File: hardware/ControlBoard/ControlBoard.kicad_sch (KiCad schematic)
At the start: 122 parts, among them J1 Lamp 1 Out, J10 CAN, J11 USB_B_Micro, J12 Conn_01x02, J13 AVAILABLE GPIO, J14 MOTOR_CTRL1, J15 MOTOR_CTRL2, J2 ESTOP1, J3 ESTOP2, J4 Lamp 3 Out, J5 Lamp 2 Out, J6 Lamp 4 Out, J7 PWR_IN, J8 USB_B_Micro, J9 UART BACKUP, Q1 2N7002, Q2 2N7002, Q3 2N7002, Q4 2N7002, Q5 SS8050-G, Q6 SS8050-G, SW1 SW_Push, SW2 SW_Push, U1 CP2102N-A02-GQFN28, U2 Lora_Module, U5 ESP32-S3-WROOM-1U, U6 74LVC1G97W6-7, U7 SN65HVD232, U8 SN74LVC1GU04DBVR

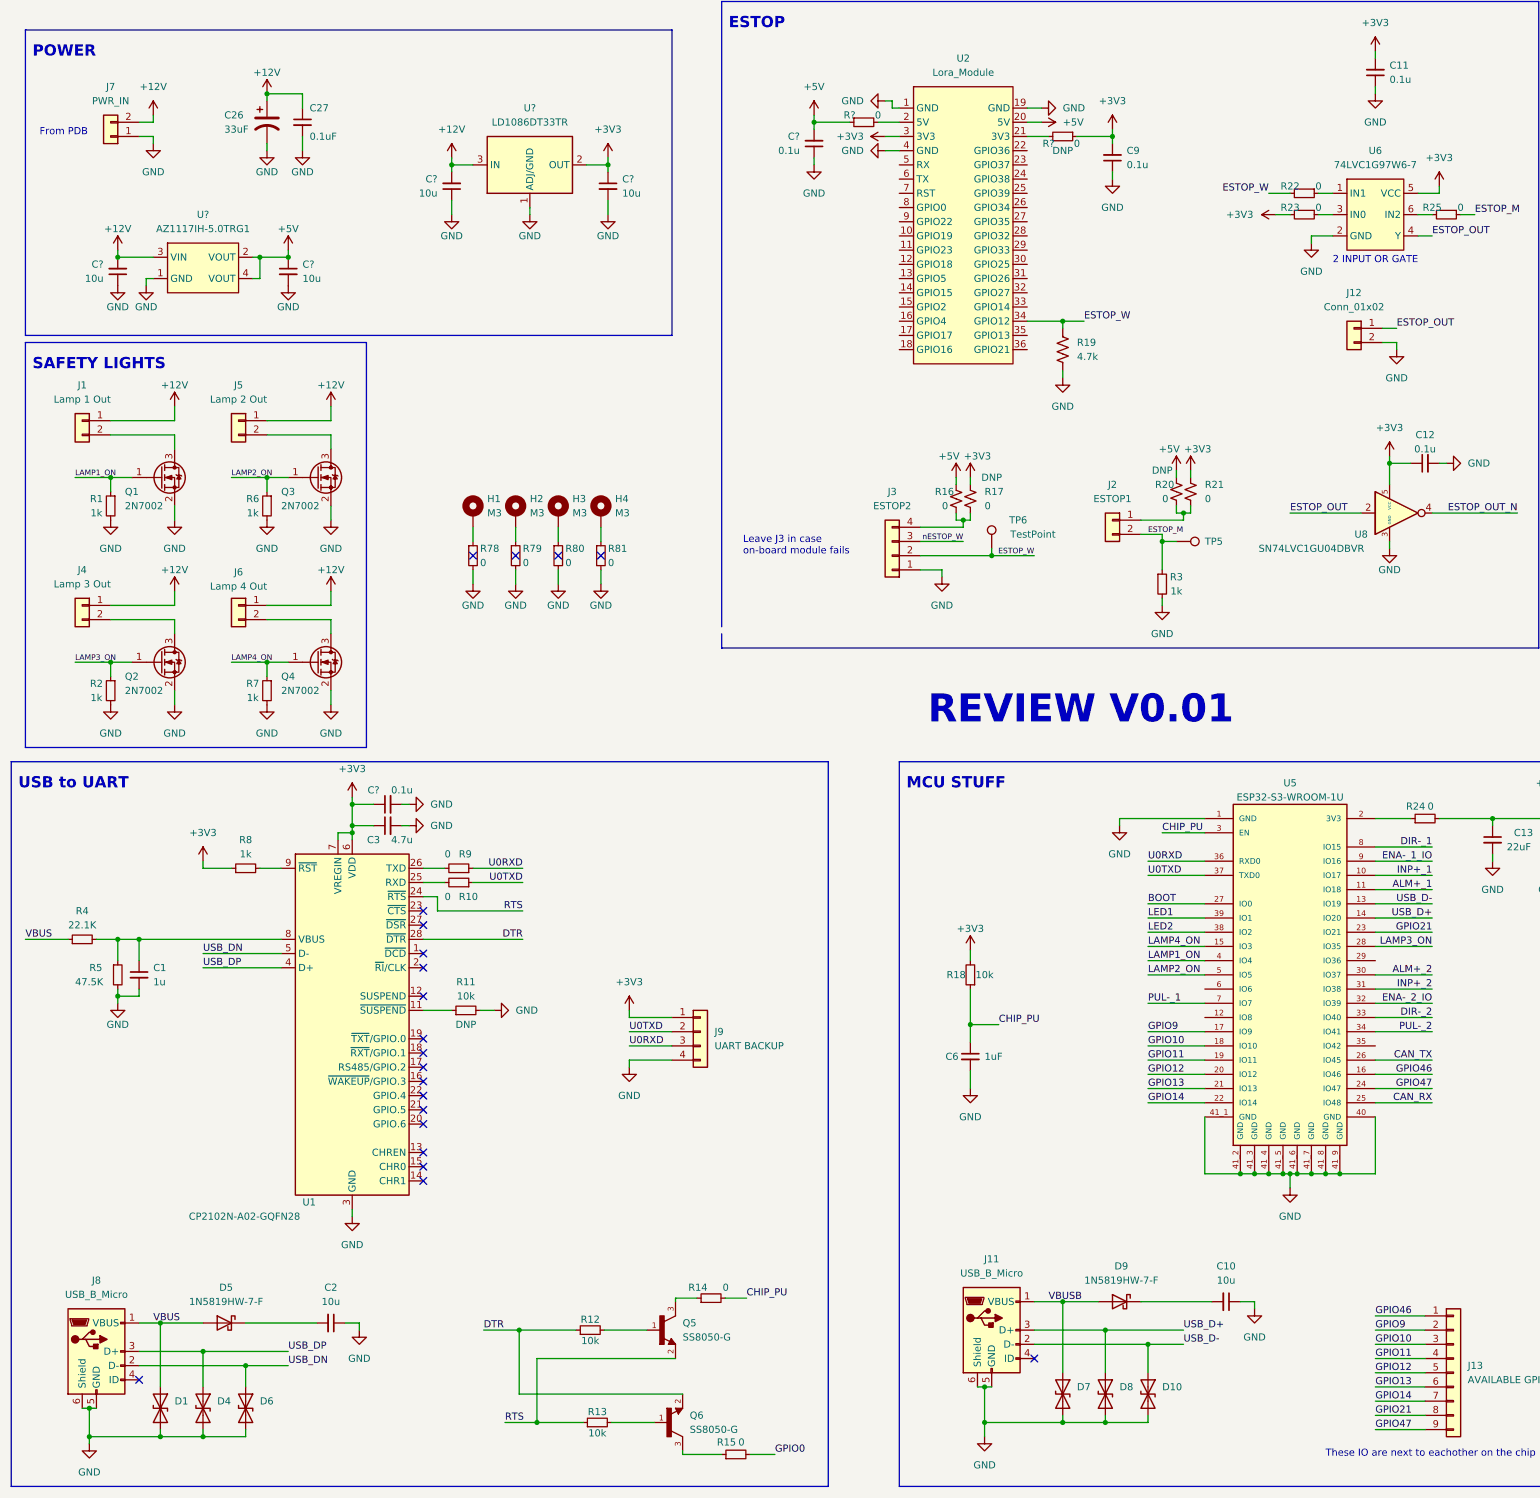
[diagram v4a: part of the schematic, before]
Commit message: Starting Control Board Layout
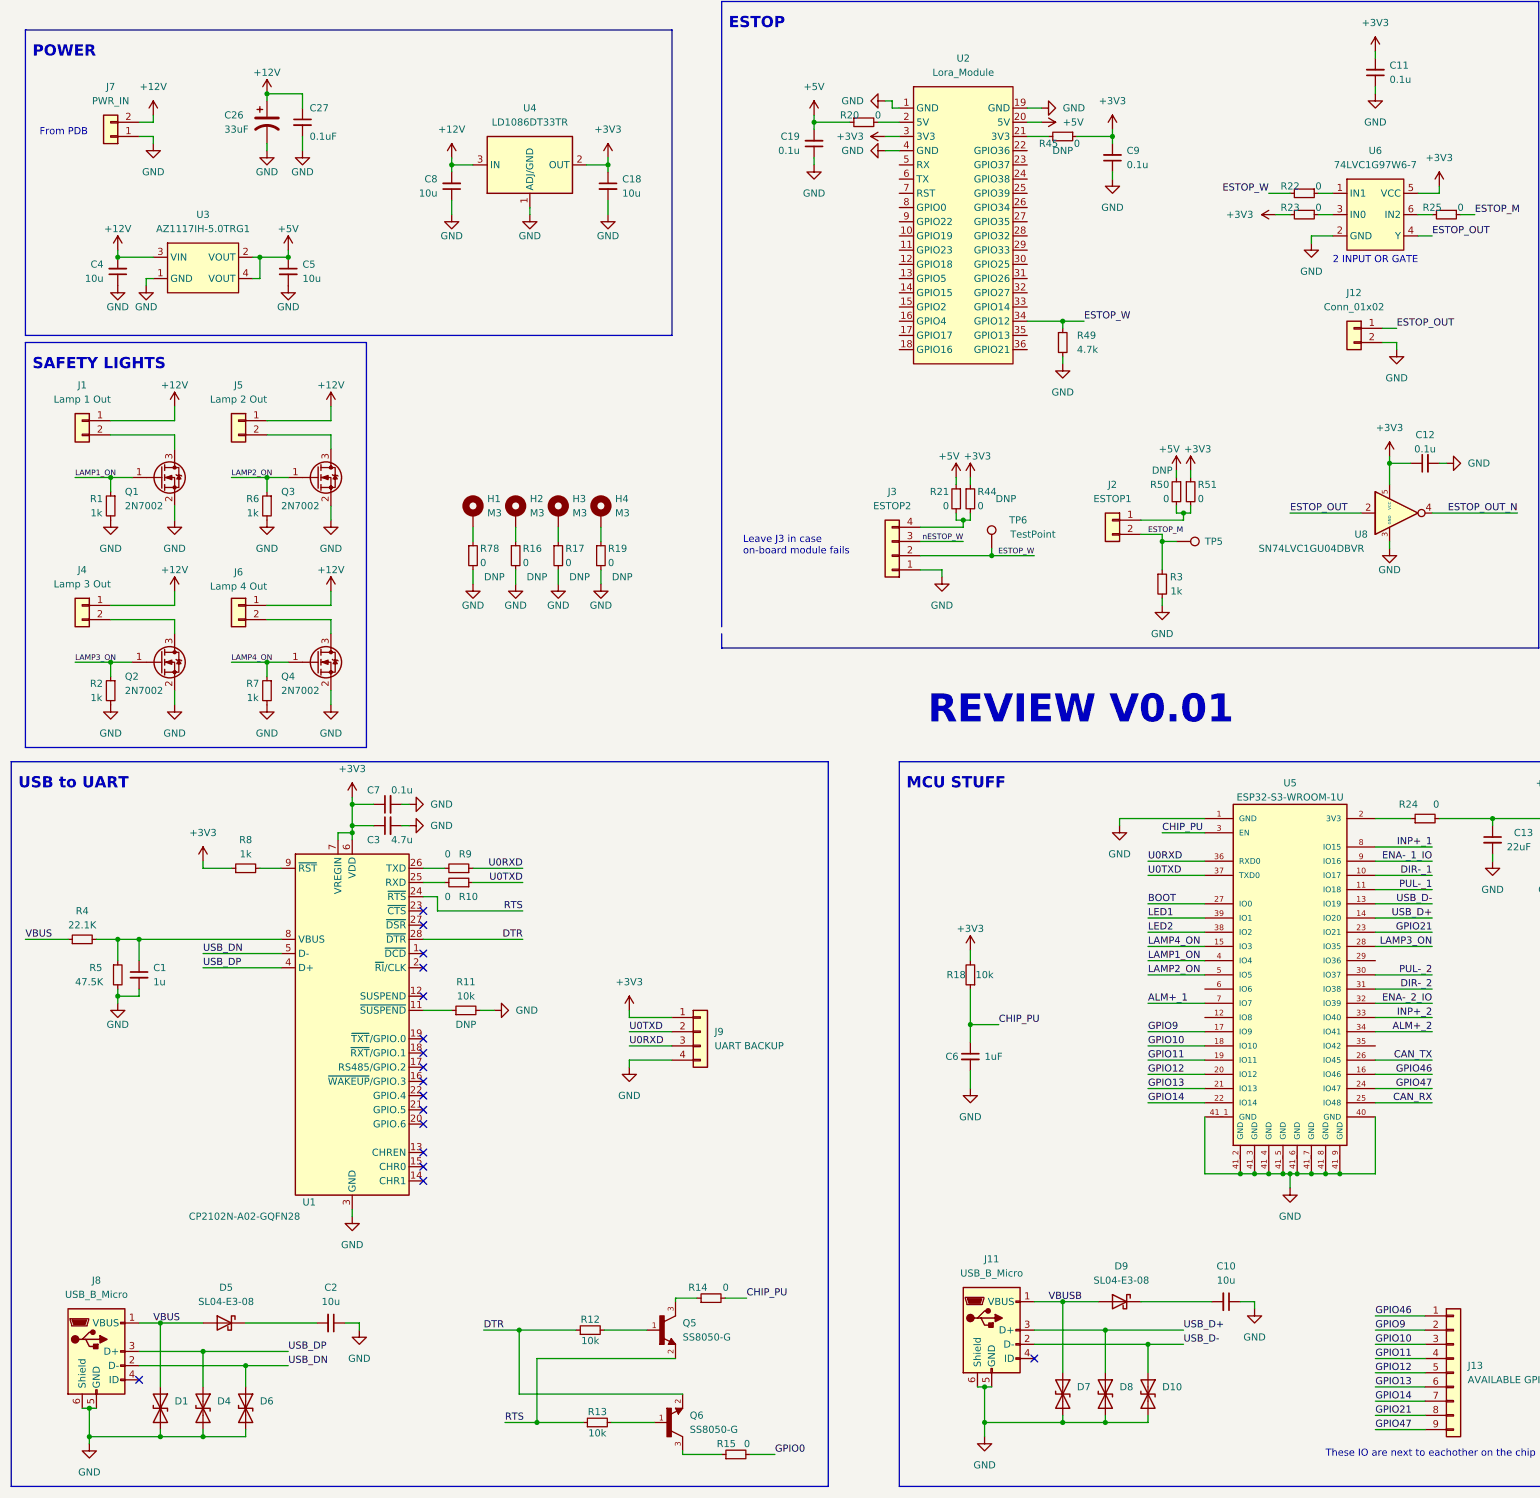
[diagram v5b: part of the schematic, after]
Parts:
- removed R16, R17, R20, R21: 0, symbol Device:R_Small_US
- removed R19: 4.7k, symbol Device:R_US
- removed R79, R80, R81: 0, Resistor_SMD:R_0603_1608Metric, symbol Device:R_Small
- added R16, R17, R19, R21, R44, R50, R51: 0, Resistor_SMD:R_0805_2012Metric, symbol Device:R_Small
- added R49: 4.7k, Resistor_SMD:R_0805_2012Metric, symbol Device:R_Small
- C1, C10, C11, C12, C2, C3, C9: footprint (none) -> Capacitor_SMD:C_0805_2012Metric
- C17: footprint Capacitor_SMD:C_0603_1608Metric -> Capacitor_SMD:C_0805_2012Metric
- C18, C19, C4, C5, C7, C8: renamed from C?; footprint (none) -> Capacitor_SMD:C_0805_2012Metric
- D5, D9: value 1N5819HW-7-F -> SL04-E3-08; footprint (none) -> Diode_SMD:D_SMF; Digikey 1N5819HW-FDICT-ND -> SL04-E3-08GICT-ND
- J11, J8: footprint (none) -> Connector_USB:USB_Micro-B_Molex-105017-0001; Digikey (none) -> WM1399CT-ND
- J7: footprint Connector_Molex:Molex_Mini-Fit_Sr_42820-22XX_1x02_P10.00mm_Horizontal -> Connector_Molex:Molex_Micro-Fit_3.0_43650-0200_1x02_P3.00mm_Horizontal; Digikey 0428202224-ND -> WM1860-ND
- R1, R10, R14, R15, R2, R24, R3, R6, R7, R75, R76, R9: footprint Resistor_SMD:R_0603_1608Metric -> Resistor_SMD:R_0805_2012Metric
- R11, R22, R23, R25, R26, R27, R28, R29, R30, R31, R32, R33, R34, R35, R36, R37, R38, R39, R4, R40, R41, R42, R43, R5, R8: footprint (none) -> Resistor_SMD:R_0805_2012Metric
- R20, R45: renamed from R?; footprint (none) -> Resistor_SMD:R_0805_2012Metric
- R46, R47: Digikey CR0603-JW-331ELFCT-ND -> (none)
- R48: footprint Resistor_SMD:R_0603_1608Metric -> Resistor_SMD:R_0805_2012Metric; Digikey A129677CT-ND -> (none)
- R78: footprint Resistor_SMD:R_0603_1608Metric -> Resistor_SMD:R_0805_2012Metric; DNP (none) -> DNP
- SW1, SW2: footprint (none) -> Button_Switch_SMD:SW_SPST_B3U-1100P-B; Digikey (none) -> SW1104CT-ND
- U6: footprint (none) -> controlLib:74LVC1G97W6-7
- gave numbers to parts that had none: 2
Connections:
- net +3V3: now also R44.1, R51.1
- net +5V: now also R21.1, R50.1
- net ALM+_1: now also U5.7 (IO7); no longer U5.11 (IO18)
- net ALM+_2: now also U5.34 (IO41); no longer U5.30 (IO37)
- net DIR-_1: now also U5.10 (IO17); no longer U5.8 (IO15)
- net DIR-_2: now also U5.31 (IO38); no longer U5.33 (IO40)
- net ESTOP_W: now also R49.1
- net GND: now also R16.2, R17.2, R19.2, R49.2
- net INP+_1: now also U5.8 (IO15); no longer U5.10 (IO17)
- net INP+_2: now also U5.33 (IO40); no longer U5.31 (IO38)
- net PUL-_1: now also U5.11 (IO18); no longer U5.7 (IO7)
- net PUL-_2: now also U5.30 (IO37); no longer U5.34 (IO41)
- net at H4.1: now also R19.1
- net at J3.4 (Pin_4): now also R21.2, R44.2
- net at H2.1: now also R16.1
- net at J2.1 (Pin_1): now also R50.2, R51.2
- net at H3.1: now also R17.1
- no-connect marks 21 -> 17

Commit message: More Layout
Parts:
- added C20, C21: 0.1u, Capacitor_SMD:C_0805_2012Metric, symbol Device:C_Small
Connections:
- net GPIO0 is gone; now on net BOOT: R15.2
- net +3V3: no longer C9.2, U2.3 (3V3)
- net +5V: no longer C19.2, U2.20 (5V)
- net ALM+_2: now also U5.30 (IO37); no longer U5.34 (IO41)
- net DIR-_2: now also U5.33 (IO40); no longer U5.31 (IO38)
- net GND: now also C20.1, C21.1
- net INP+_2: now also U5.31 (IO38); no longer U5.33 (IO40)
- net LAMP3_ON: now also U5.38 (IO2); no longer U5.28 (IO35)
- net LAMP4_ON: now also U5.39 (IO1); no longer U5.15 (IO3)
- net LED1: now also U5.15 (IO3); no longer U5.39 (IO1)
- net LED2: now also U5.28 (IO35); no longer U5.38 (IO2)
- net PUL-_2: now also U5.34 (IO41); no longer U5.30 (IO37)
- net 5V_LORA: now reaches R20.2, U2.2 (5V)
- net 5V_LORA: now also C9.2, U2.20 (5V), C20.2
- net 3V3_LORA: now reaches R45.2, U2.21 (3V3)
- net 3V3_LORA: now also C19.2, U2.3 (3V3), C21.2
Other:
- moved on the sheet: C19, C9, R20, R45

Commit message: Start Control Board Routing
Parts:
- removed J13: AVAILABLE GPIO, Connector_PinHeader_2.54mm:PinHeader_1x09_P2.54mm_Vertical, symbol Connector_Generic:Conn_01x09
- added J13: AVAILABLE GPIO, Connector_PinHeader_1.27mm:PinHeader_1x08_P1.27mm_Vertical, symbol Connector_Generic:Conn_01x08
- added TP1, TP2, TP3, TP4: TestPoint, TestPoint:TestPoint_Pad_D1.0mm, symbol Connector:TestPoint
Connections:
- net GPIO46 is gone; now on net ESTOP_OUT: U5.16 (IO46)
- net +12V: now also TP1.1
- net +3V3: now also TP3.1
- net +5V: now also TP2.1
- net ESTOP_OUT: now also TP4.1
- net GPIO10: now also J13.2 (Pin_2)
- net GPIO11: now also J13.3 (Pin_3)
- net GPIO12: now also J13.4 (Pin_4)
- net GPIO13: now also J13.5 (Pin_5)
- net GPIO14: now also J13.6 (Pin_6)
- net GPIO21: now also J13.7 (Pin_7)
- net GPIO47: now also J13.8 (Pin_8)
- net GPIO9: now also J13.1 (Pin_1)
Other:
- moved on the sheet: C4, C5

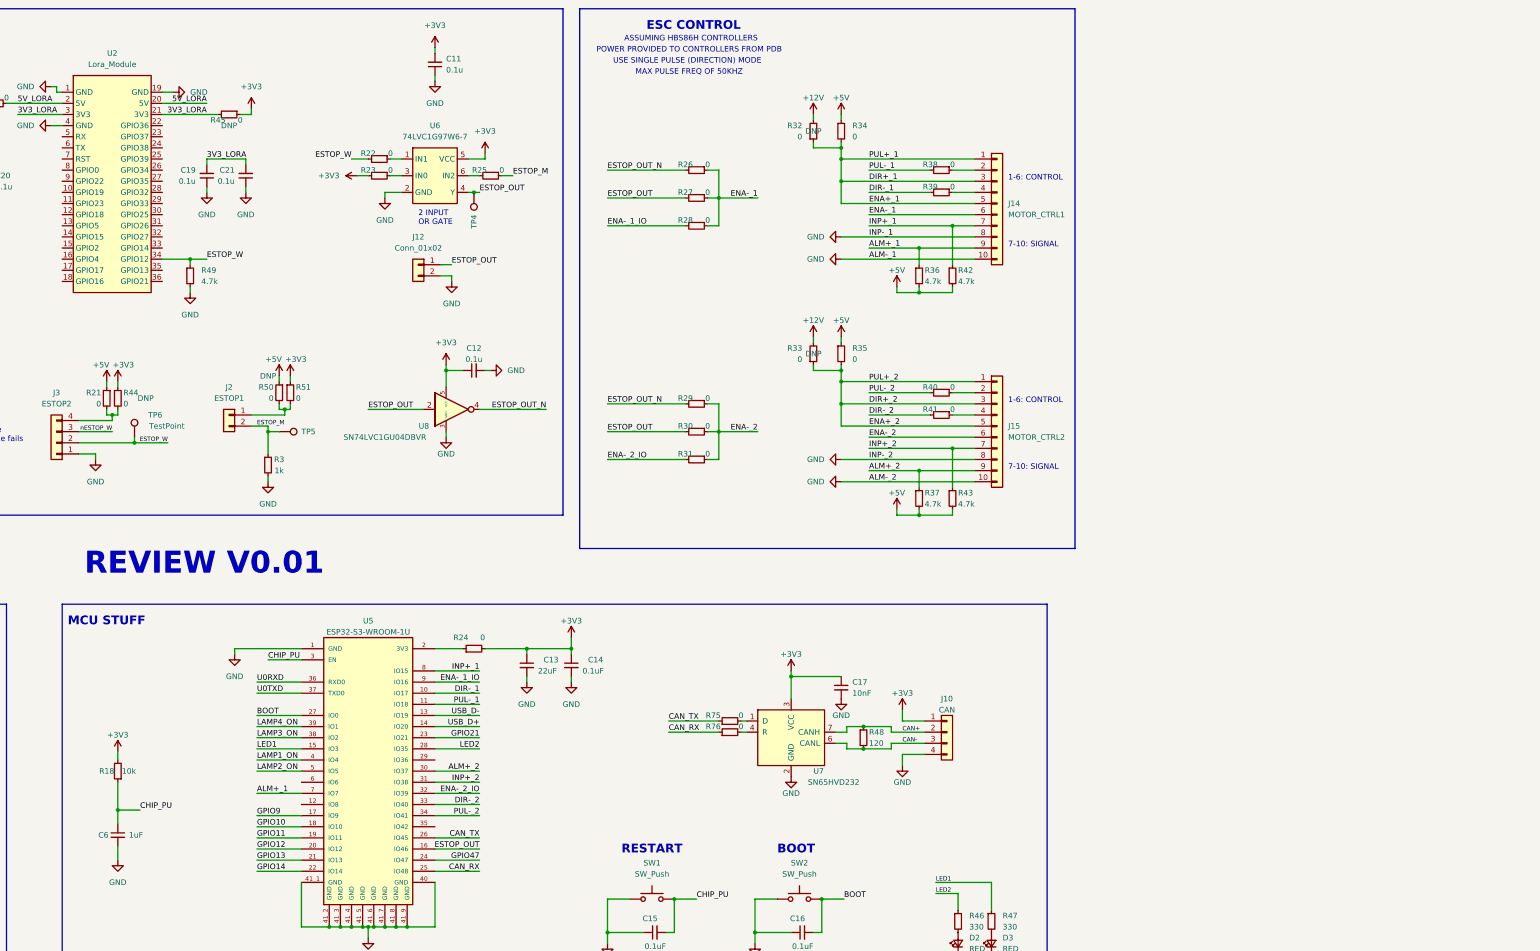
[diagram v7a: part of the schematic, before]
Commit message: Motor Controller IO Fixes
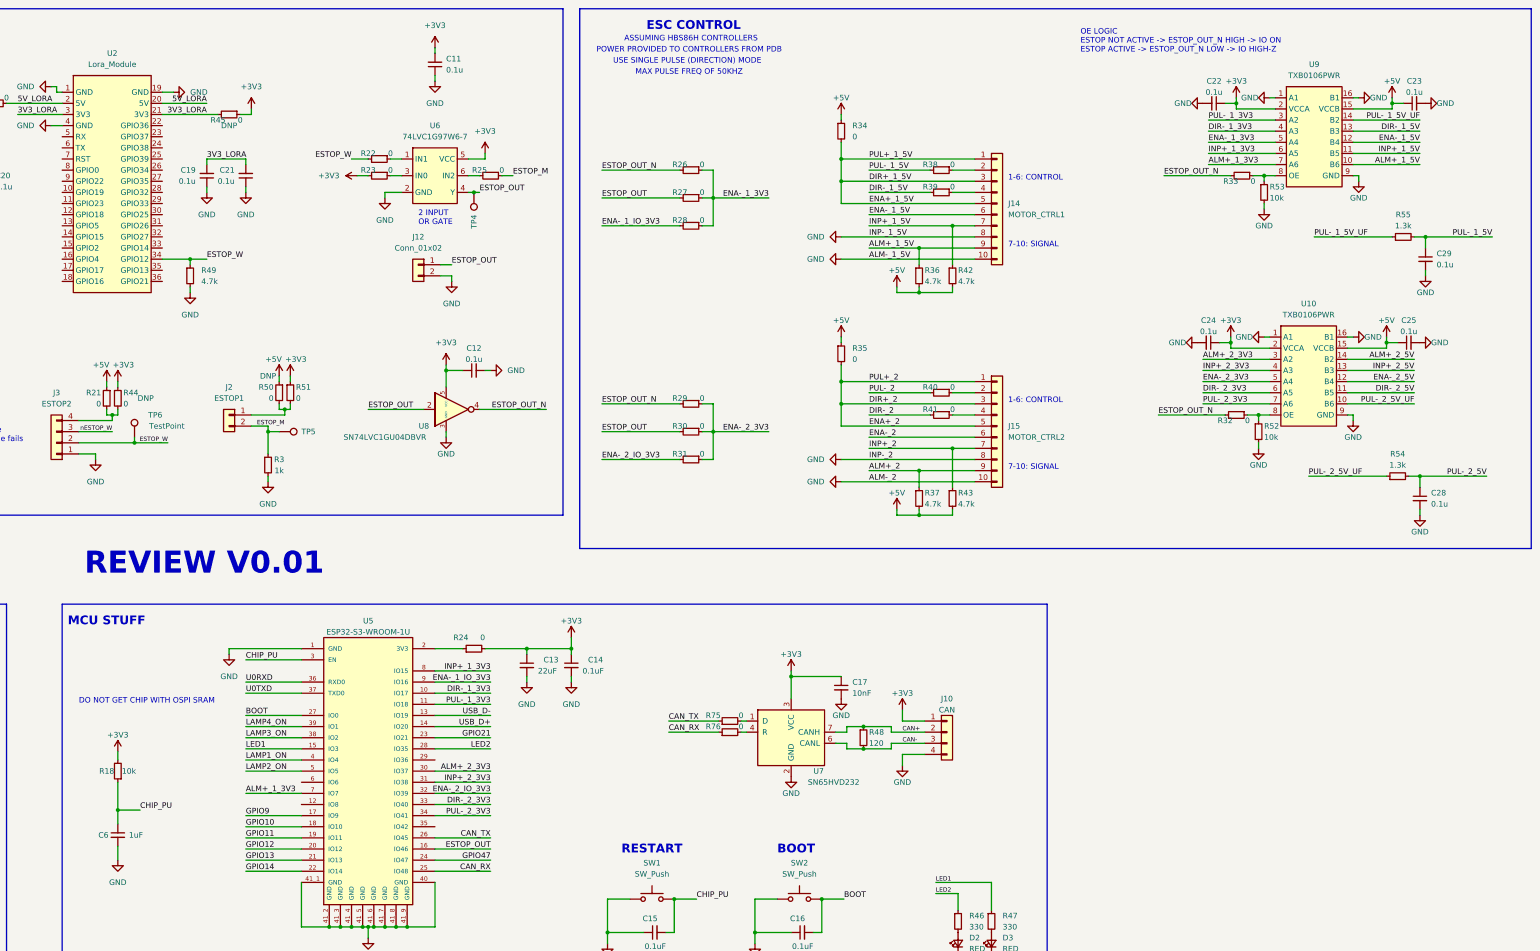
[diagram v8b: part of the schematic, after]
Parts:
- added C22, C23, C24, C25, C28, C29: 0.1u, Capacitor_SMD:C_0805_2012Metric, symbol Device:C_Small
- added R52, R53: 10k, Resistor_SMD:R_0805_2012Metric, symbol Device:R_Small
- added R54, R55: 1.3k, Resistor_SMD:R_0805_2012Metric, symbol Device:R_Small
- added U10, U9: TXB0106PWR, controlLib:TXB0106PWR, symbol controlLib:TXB0106PWR
- R32, R33: DNP DNP -> (none)
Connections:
- net +12V: no longer R32.2, R33.2
- net +3V3: now also C22.1, C24.1, U10.2 (VCCA), U9.2 (VCCA)
- net +5V: now also C23.1, C25.1, U10.15 (VCCB), U9.15 (VCCB)
- net ALM+_2: no longer U5.30 (IO37)
- net DIR+_2: no longer R33.1
- net DIR-_2: no longer U5.33 (IO40)
- net ENA-_2: no longer R29.1, R30.1, R31.1
- net ESTOP_OUT_N: now also R32.2, R33.2
- net GND: now also C22.2, C23.2, C24.2, C25.2, C28.2, C29.2, R52.2, R53.2, U10.1 (A1), U10.16 (B1), U10.9 (GND), U9.1 (A1), U9.16 (B1), U9.9 (GND)
- net INP+_2: no longer U5.31 (IO38)
- net PUL-_2: no longer U5.34 (IO41)
- net ALM+_1 renamed ALM+_1_5V
- net ALM+_1_5V: now also U9.10 (B6); no longer U5.7 (IO7)
- net DIR+_1 renamed DIR+_1_5V
- net DIR+_1_5V: no longer R32.1
- net DIR-_1 renamed DIR-_1_3V3
- net DIR-_1_3V3: now also U9.4 (A3); no longer R39.2
- net ENA-_1 renamed ENA-_1_3V3
- net ENA-_1_3V3: now also U9.5 (A4); no longer J14.6 (Pin_6)
- net ENA-_1_IO renamed ENA-_1_IO_3V3
- net ENA-_2_IO renamed ENA-_2_IO_3V3
- net INP+_1 renamed INP+_1_5V
- net INP+_1_5V: now also U9.11 (B5); no longer U5.8 (IO15)
- net PUL-_1 renamed PUL-_1_3V3
- net PUL-_1_3V3: now also U9.3 (A2); no longer R38.2
- new net: R32.1, R52.1, U10.8 (OE)
- new net: R33.1, R53.1, U9.8 (OE)
- new net ALM+_1_3V3: U5.7 (IO7), U9.7 (A6)
- new net ALM+_2_3V3: U10.3 (A2), U5.30 (IO37)
- new net ALM+_2_5V: U10.14 (B2)
- new net DIR-_1_5V: R39.2, U9.13 (B3)
- new net DIR-_2_3V3: U10.6 (A5), U5.33 (IO40)
- new net DIR-_2_5V: U10.11 (B5)
- new net ENA-_1_5V: J14.6 (Pin_6), U9.12 (B4)
- new net ENA-_2_3V3: R29.1, R30.1, R31.1, U10.5 (A4)
- new net ENA-_2_5V: U10.12 (B4)
- new net INP+_1_3V3: U5.8 (IO15), U9.6 (A5)
- new net INP+_2_3V3: U10.4 (A3), U5.31 (IO38)
- new net INP+_2_5V: U10.13 (B3)
- new net PUL-_1_5V: C29.1, R38.2, R55.2
- new net PUL-_1_5V_UF: R55.1, U9.14 (B2)
- new net PUL-_2_3V3: U10.7 (A6), U5.34 (IO41)
- new net PUL-_2_5V: C28.1, R54.2
- new net PUL-_2_5V_UF: R54.1, U10.10 (B6)
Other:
- note added: "DO NOT GET CHIP WITH OSPI SRAM"
- note added: "OE LOGIC ESTOP NOT ACTIVE -> ESTOP_OUT_N HIGH -> IO ON ESTOP ACTIVE -> ESTOP_OUT_N LOW -> IO HIGH-Z"
- moved on the sheet: R26, R27, R28, R29, R30, R31
